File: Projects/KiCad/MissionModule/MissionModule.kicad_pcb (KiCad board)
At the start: 2 copper layers, 110 x 95 mm, 53 parts, among them J1 Conn_01x08, J2 Micro_SD_Card_Det_Hirose_DM3AT, SW1 SW_Push, SW2 SW_Push, U1 MCP2562-E-P, U2 MCP2515-I/P, U3 NJM7805SDL1, U5 TLP222A, U6 ABX00012, U7 MB85RS2MT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

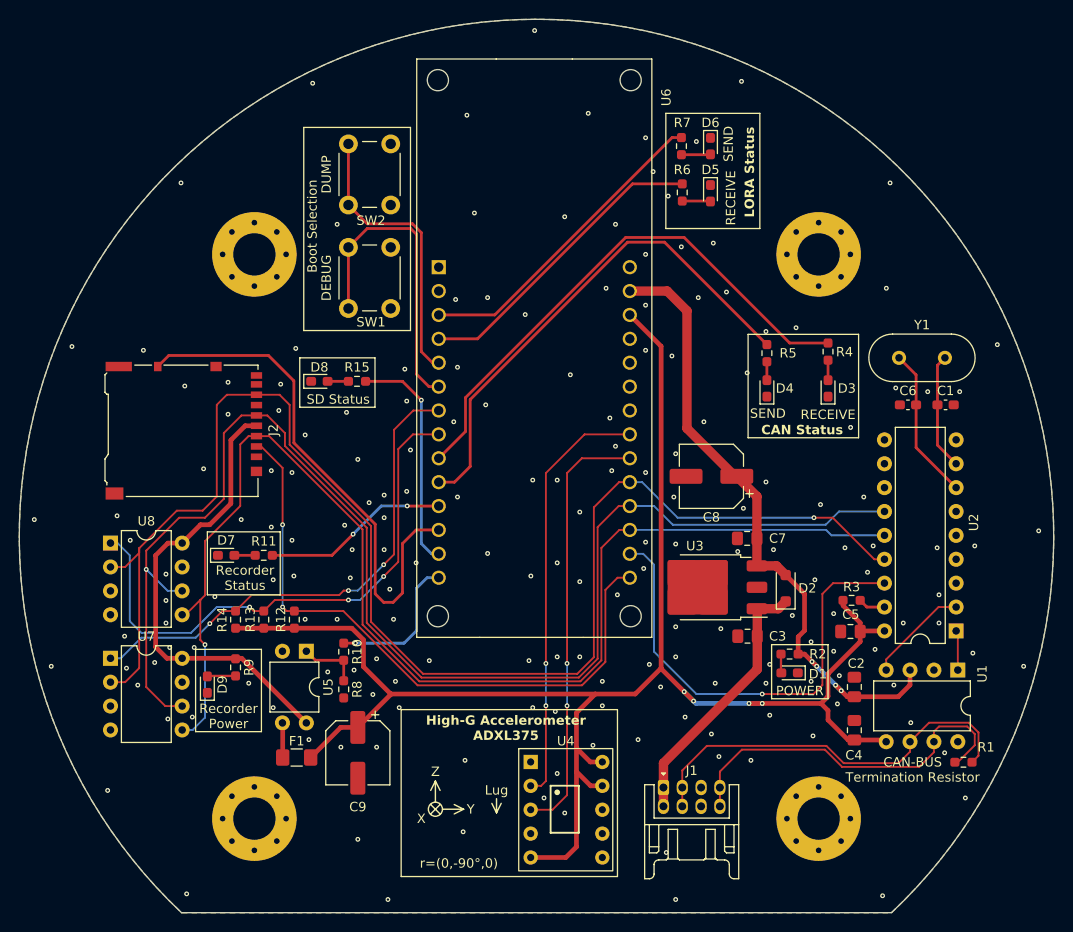
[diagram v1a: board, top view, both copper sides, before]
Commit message: 穴径を調整
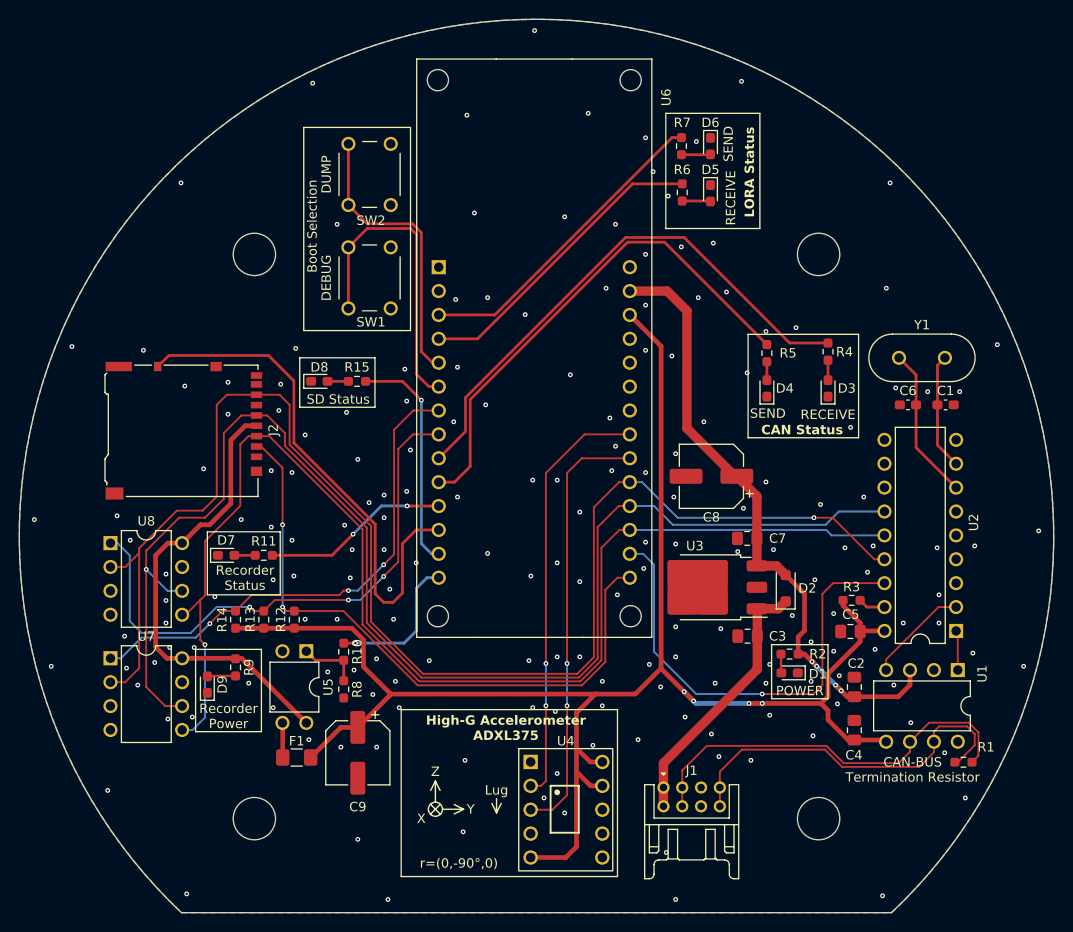
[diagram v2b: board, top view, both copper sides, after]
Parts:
- REF** (x4): value MountingHole_4.5mm_Pad_Via -> MountingHole_4.5mm; footprint MountingHole:MountingHole_4.5mm_Pad_Via -> MountingHole:MountingHole_4.5mm

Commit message: テストポイントを追加
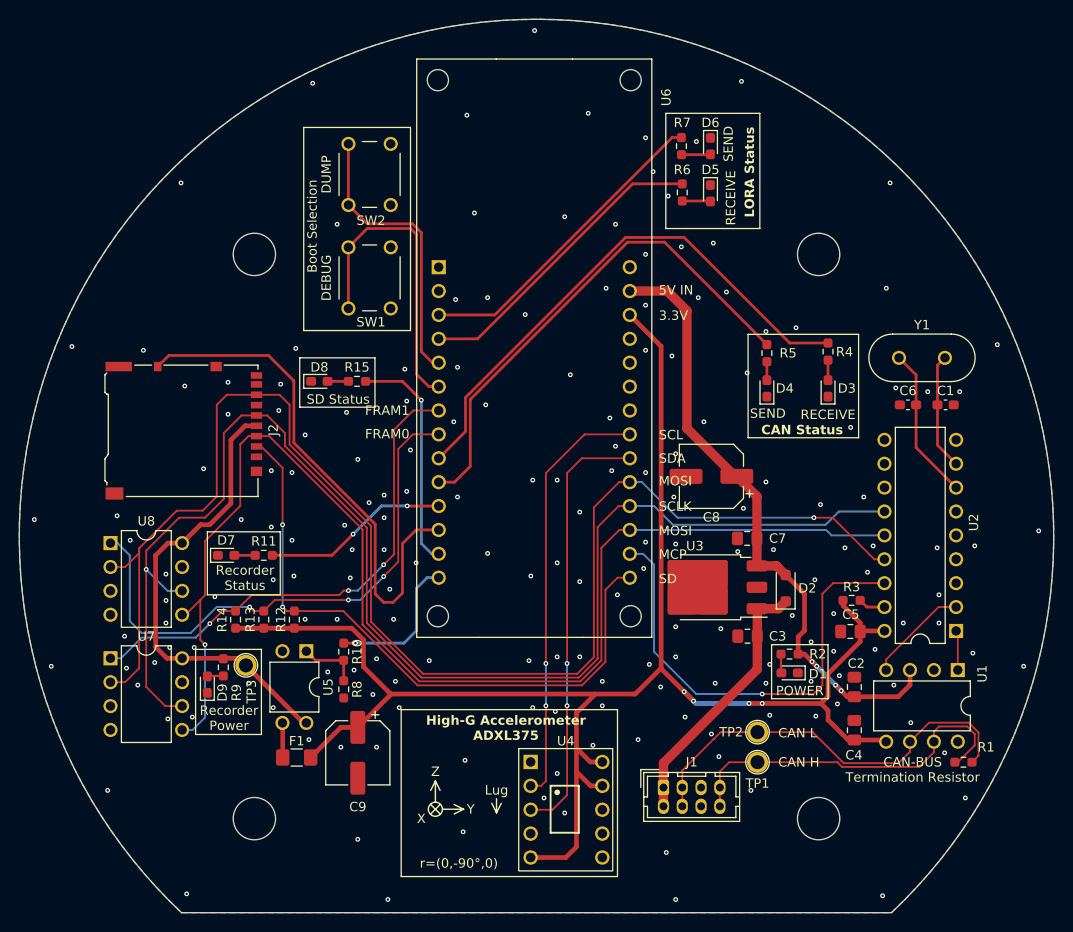
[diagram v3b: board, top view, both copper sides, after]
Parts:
- added TP1: TestPoint, Connector_Pin:Pin_D1.0mm_L10.0mm, F.Cu at (172.0, 129.0)
- added TP2: TestPoint, Connector_Pin:Pin_D1.0mm_L10.0mm, F.Cu at (172.0, 125.8)
- added TP3: TestPoint, Connector_Pin:Pin_D1.0mm_L10.0mm, F.Cu at (117.6, 118.7)
- J1: footprint Hirose_Connector:Hirose_DF11B-8DP-2DS -> Connector_Hirose:Hirose_DF11-8DP-2DSA_2x04_P2.00mm_Vertical
- moved R9 1.30 mm to (115.2, 118.9)
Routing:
- net Net-(D9-A): track 2.95 -> 1.65 mm
- net CAN_L: track 43.4 -> 44.7 mm
- net CAN_H: track 39.7 -> 38.6 mm
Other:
- board text added: "3.3V"
- board text added: "5V IN"
- board text added: "CAN H"
- board text added: "CAN L"
- board text added: "FRAM0"
- board text added: "FRAM1"
- board text added: "MCP"
- board text added: "MOSI"
- board text added: "SCL"
- board text added: "SCLK"
- board text added: "SD"
- board text added: "SDA"

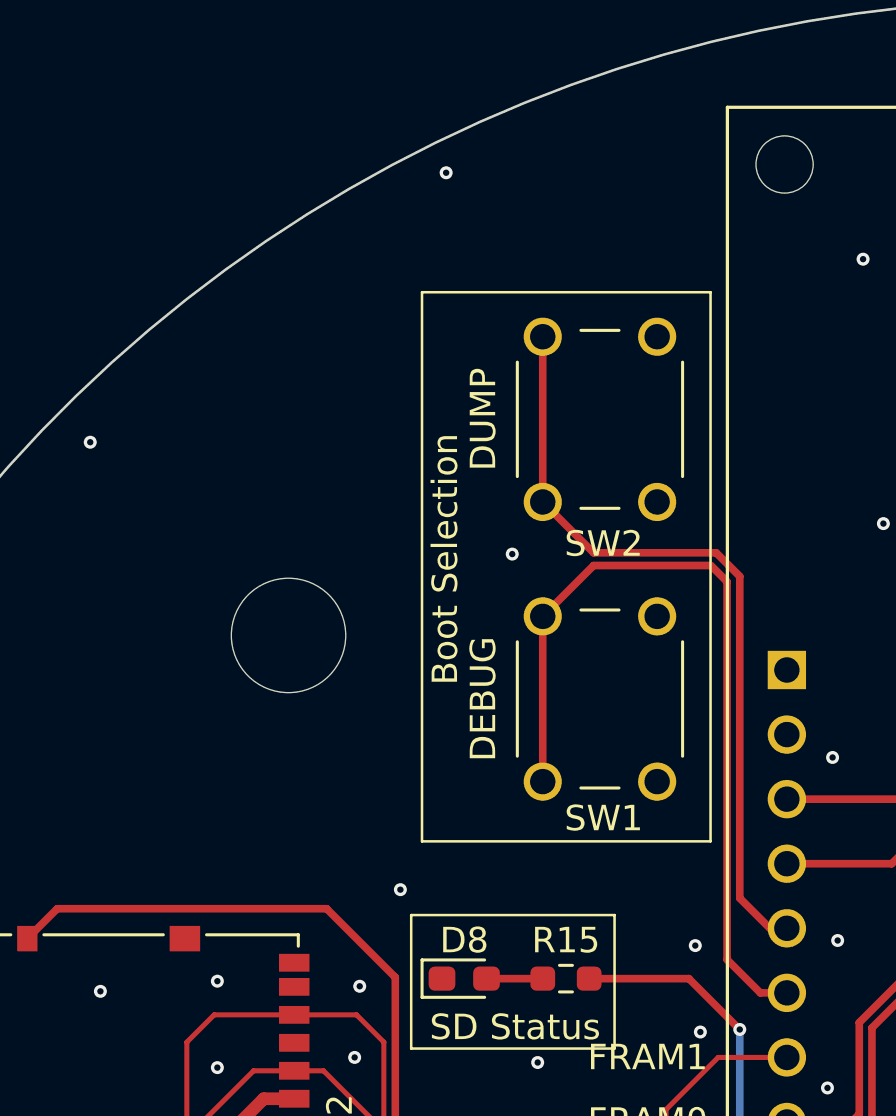
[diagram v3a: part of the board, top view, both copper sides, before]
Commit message: スイッチをピアノスイッチに変更
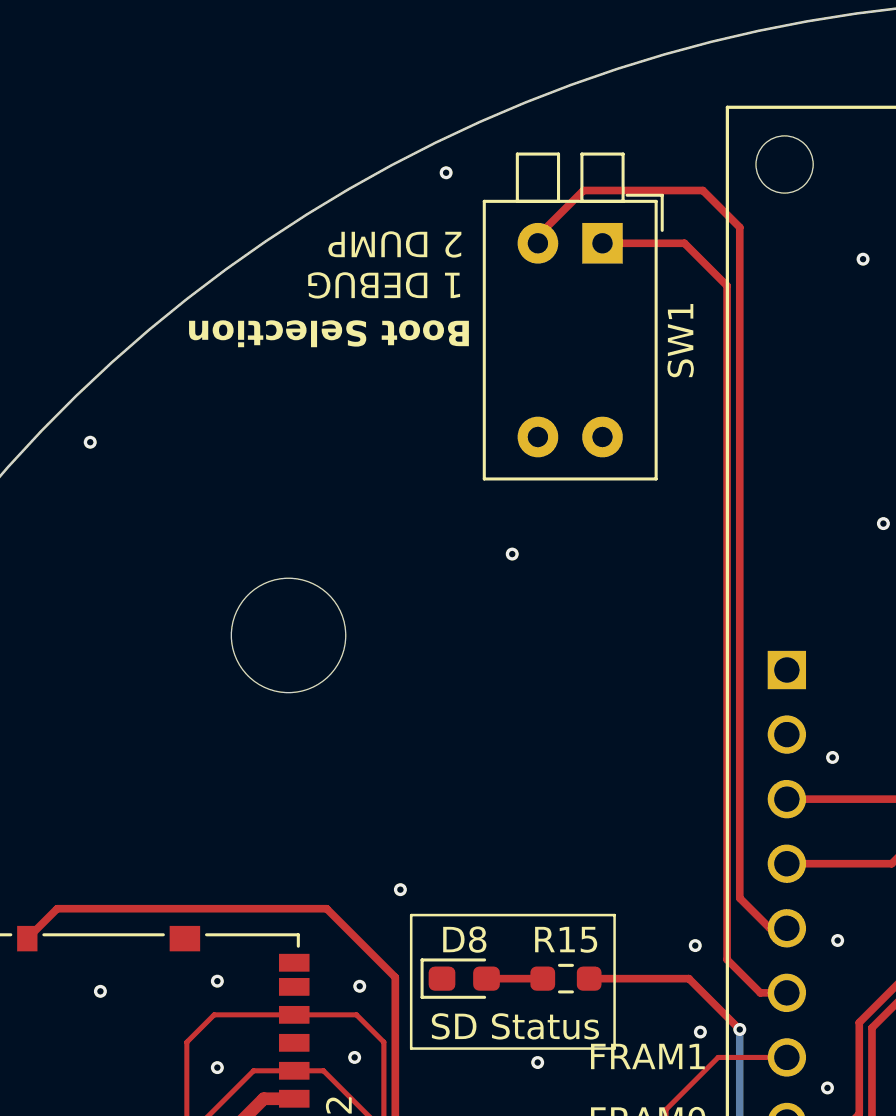
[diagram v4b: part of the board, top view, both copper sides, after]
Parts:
- removed SW2: SW_Push, Button_Switch_THT:SW_PUSH_6mm
- SW1: value SW_Push -> SW_DIP_x02; footprint Button_Switch_THT:SW_PUSH_6mm -> Button_Switch_THT:SW_DIP_SPSTx02_Piano_10.8x6.64mm_W7.62mm_P2.54mm
- moved SW1 14.8 mm to (130.8, 59.6)
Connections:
- SW1 pad 1: GND -> DEBUG_MODE
- SW1 pad 2: DEBUG_MODE -> DUMP_MODE
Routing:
- net DUMP_MODE: track 30.5 -> 38.3 mm
- net DEBUG_MODE: track 32.6 -> 35.0 mm
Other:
- board text added: "1 DEBUG 2 DUMP"
- board text removed: "DEBUG"
- board text removed: "DUMP"

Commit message: ベタを修正
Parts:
- moved C8 6.71 mm to (173.7, 99.8), turned to 0 degrees
- moved C7 4.41 mm to (171.2, 109.6)
- moved U3 3.90 mm to (167.0, 114.3)
- moved C3 3.42 mm to (170.6, 119.0)
- moved R15 2.93 mm to (132.0, 87.1)
- moved D8 2.93 mm to (128.0, 87.1)
- moved D2 2.78 mm to (175.2, 113.3)
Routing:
- net +12V: track 28.5 -> 25.1 mm
- net SD_STATUS: track 24.3 -> 22.3 mm
- net +5V: track 67.5 -> 68.7 mm
- net SPI_CS_MCP: track 49.2 -> 48.7 mm
- net GND: vias 187 -> 188

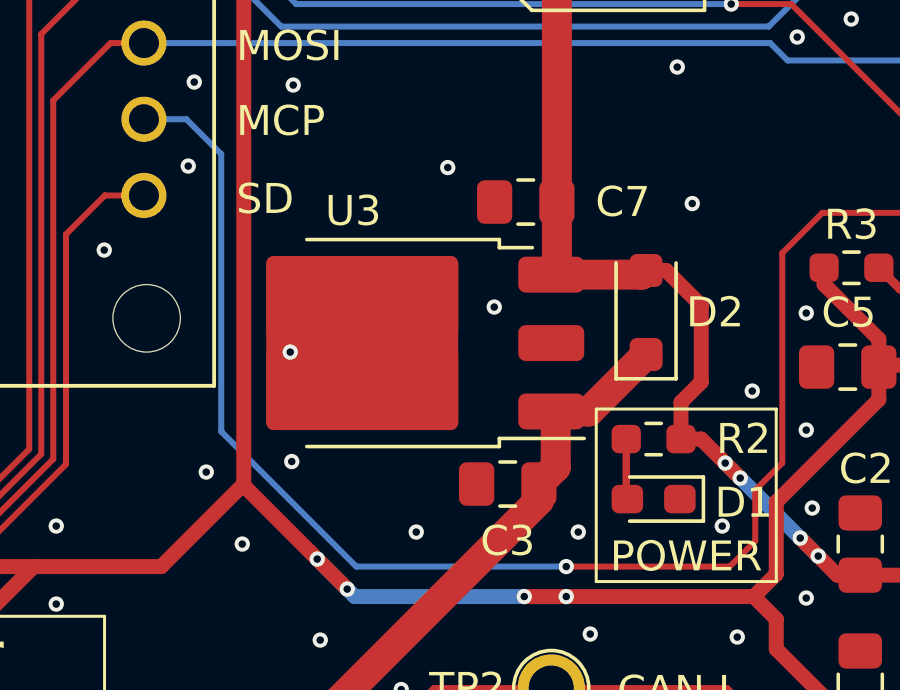
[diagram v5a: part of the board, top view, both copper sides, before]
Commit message: 三端子レギュレータをTO-252-3からTO-252-2に変更
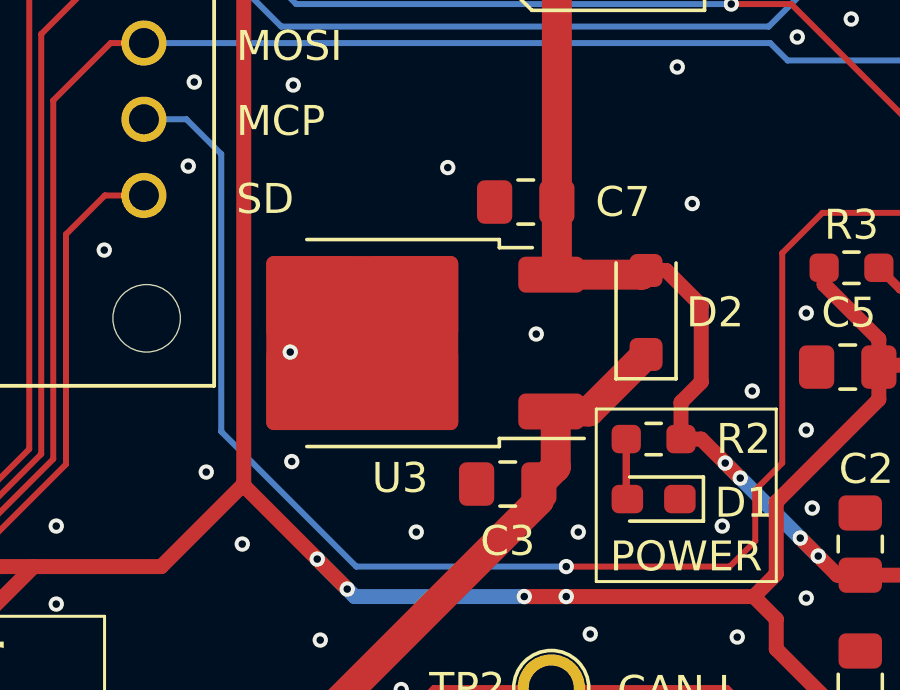
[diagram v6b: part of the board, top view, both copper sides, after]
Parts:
- U3: footprint Package_TO_SOT_SMD:TO-252-3_TabPin2 -> Package_TO_SOT_SMD:TO-252-2
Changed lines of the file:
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@@
     (descr "2x-dip-switch SPST , Piano, row spacing 7.62 mm (300 mils), body size 10.8x6.64mm")
     (tags "DIP Switch SPST Piano 7.62mm 300mil")
-    (property "Sheetfile" "SensingModule.kicad_sch")
+    (property "Sheetfile" "MissionModule.kicad_sch")
     (property "Sheetname" "")
     (property "ki_description" "2x DIP Switch, Single Pole Single Throw (SPST) switch, small symbol")
@@
       (net 54 "unconnected-(U6-+5V-Pad28)") (pinfunction "+5V") (pintype "power_in+no_connect"))
   )
-  (footprint "Package_TO_SOT_SMD:TO-252-3_TabPin2" (layer "F.Cu")
+  (footprint "Package_TO_SOT_SMD:TO-252-2" (layer "F.Cu")
     (at 166.96 114.299432 180)
     (descr "TO-252/DPAK SMD package, http://www.infineon.com/cms/en/product/packages/PG-TO252/PG-TO252-3-1/")
@@
     (property "ki_keywords" "Voltage Regulator 1.5A Positive")
     (attr smd)
-    (fp_text reference "U3" (at 1.56 4.4) (layer "F.SilkS")
+    (fp_text reference "U3" (at 0 -4.5 180) (layer "F.SilkS")
         (effects (font (size 1 1) (thickness 0.15)))
     )
-    (fp_text value "NJM7805SDL1" (at 0 4.5) (layer "F.Fab")
+    (fp_text value "NJM7805SDL1" (at 0 4.5 180) (layer "F.Fab")
         (effects (font (size 1 1) (thickness 0.15)))
     )
-    (fp_text user "${REFERENCE}" (at 0 0) (layer "F.Fab")
+    (fp_text user "${REFERENCE}" (at 0 0 180) (layer "F.Fab")
         (effects (font (size 1 1) (thickness 0.15)))
     )
@@
     (fp_line (start -5.81 -1.905) (end -3.11 -1.905)
       (stroke (width 0.1) (type solid)) (layer "F.Fab"))
-    (fp_line (start -5.81 -0.375) (end -5.81 0.375)
-      (stroke (width 0.1) (type solid)) (layer "F.Fab"))
-    (fp_line (start -5.81 0.375) (end -3.11 0.375)
-      (stroke (width 0.1) (type solid)) (layer "F.Fab"))
     (fp_line (start -5.81 1.905) (end -5.81 2.655)
       (stroke (width 0.1) (type solid)) (layer "F.Fab"))
@@
     (fp_line (start -3.11 -2.25) (end -2.11 -3.25)
       (stroke (width 0.1) (type solid)) (layer "F.Fab"))
-    (fp_line (start -3.11 -0.375) (end -5.81 -0.375)
-      (stroke (width 0.1) (type solid)) (layer "F.Fab"))
     (fp_line (start -3.11 1.905) (end -5.81 1.905)
       (stroke (width 0.1) (type solid)) (layer "F.Fab"))
@@
     (pad "1" smd roundrect (at -5.04 -2.28 180) (size 2.2 1.2) (layers "F.Cu" "F.Paste" "F.Mask") (roundrect_rratio 0.208333)
       (net 60 "+12V") (pinfunction "IN") (pintype "power_in"))
-    (pad "2" smd roundrect (at -5.04 0 180) (size 2.2 1.2) (layers "F.Cu" "F.Paste" "F.Mask") (roundrect_rratio 0.208333)
-      (net 2 "GND") (pinfunction "GND") (pintype "power_in"))
     (pad "2" smd roundrect (at -0.415 -1.525 180) (size 3.05 2.75) (layers "F.Cu" "F.Paste") (roundrect_rratio 0.090909)
       (net 2 "GND") (pinfunction "GND") (pintype "power_in"))
@@
     (pad "3" smd roundrect (at -5.04 2.28 180) (size 2.2 1.2) (layers "F.Cu" "F.Paste" "F.Mask") (roundrect_rratio 0.208333)
       (net 3 "+5V") (pinfunction "OUT") (pintype "power_out"))
-    (model "${KICAD6_3DMODEL_DIR}/Package_TO_SOT_SMD.3dshapes/TO-252-3_TabPin2.wrl"
+    (model "${KICAD6_3DMODEL_DIR}/Package_TO_SOT_SMD.3dshapes/TO-252-2.wrl"
       (offset (xyz 0 0 0))
       (scale (xyz 1 1 1))
@@
   (via (at 180.2 104.099432) (size 0.51) (drill 0.25) (layers "F.Cu" "B.Cu") (free) (net 2))
   (via (at 117.9 120.6) (size 0.51) (drill 0.25) (layers "F.Cu" "B.Cu") (free) (net 2))
-  (via (at 170.1 113.099432) (size 0.51) (drill 0.25) (layers "F.Cu" "B.Cu") (free) (net 2))
+  (via (at 171.5 113.999432) (size 0.51) (drill 0.25) (layers "F.Cu" "B.Cu") (free) (net 2))
   (via (at 132.7 143.6) (size 0.51) (drill 0.25) (layers "F.Cu" "B.Cu") (free) (net 2))
   (via (at 152.1 87.8) (size 0.51) (drill 0.25) (layers "F.Cu" "B.Cu") (free) (net 2))

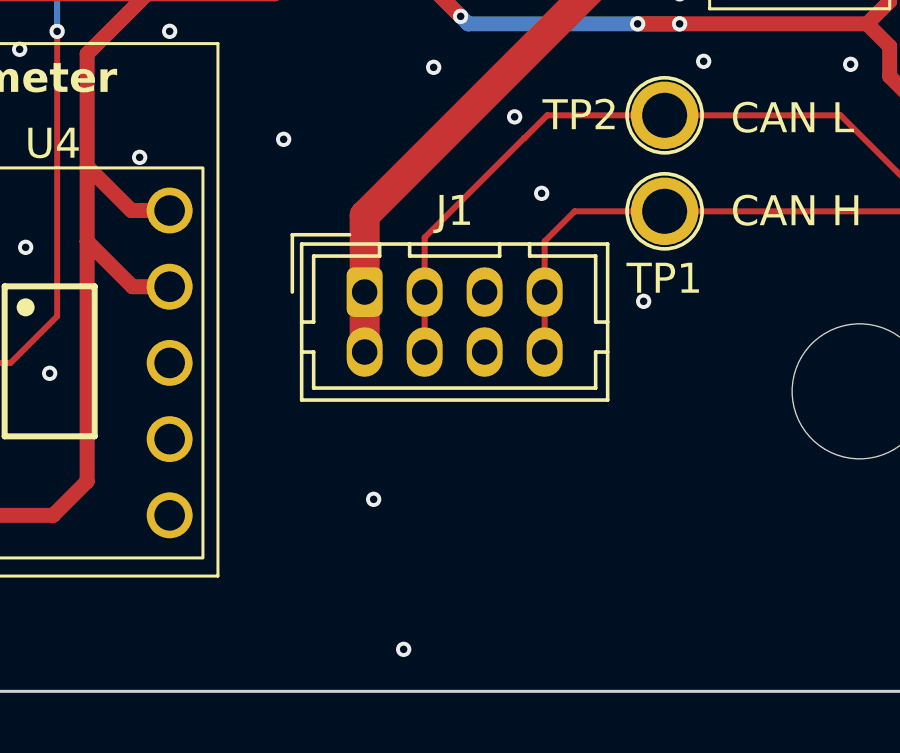
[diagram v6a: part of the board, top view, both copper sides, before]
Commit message: STEPファイルを再生成
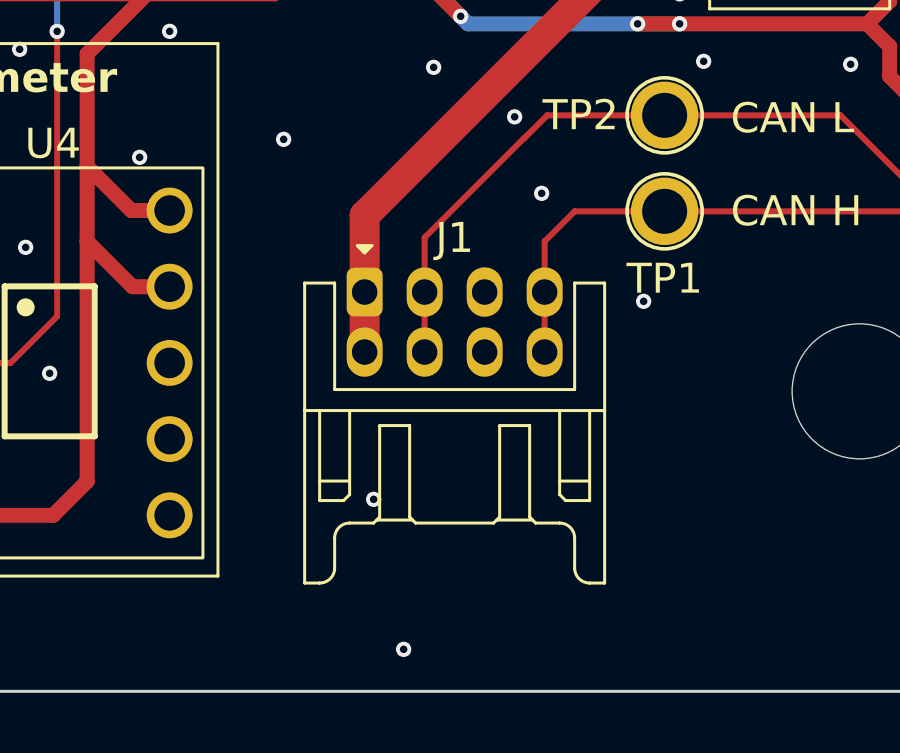
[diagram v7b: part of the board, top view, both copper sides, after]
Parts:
- J1: footprint Connector_Hirose:Hirose_DF11-8DP-2DSA_2x04_P2.00mm_Vertical -> Hirose_Connector:Hirose_DF11B-8DP-2DS
